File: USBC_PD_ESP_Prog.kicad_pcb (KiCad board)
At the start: 2 copper layers, 25 x 25 mm, 16 parts, among them J1 USB_C_Receptacle, J2 Conn_02x06_Counter_Clockwise, Q1 BC847, Q2 BC847, U1 FUSB302B01MPX, U2 CH340C, U3 NCP1117-3.3_SOT223

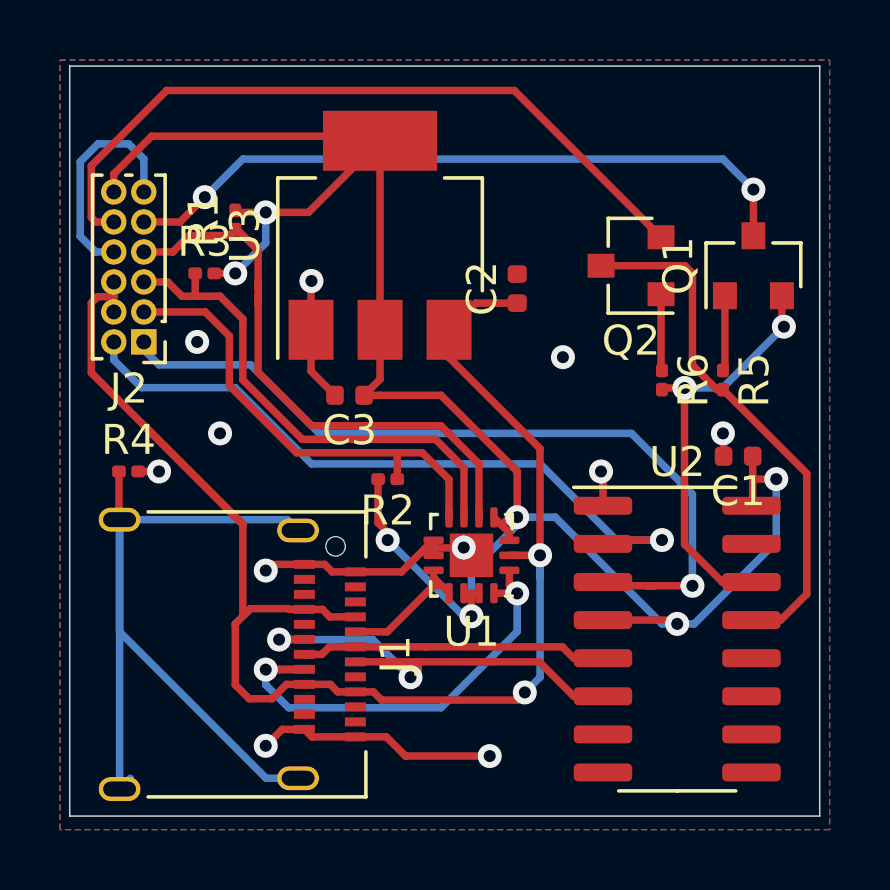
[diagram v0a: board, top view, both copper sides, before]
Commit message: Clean silkscreen
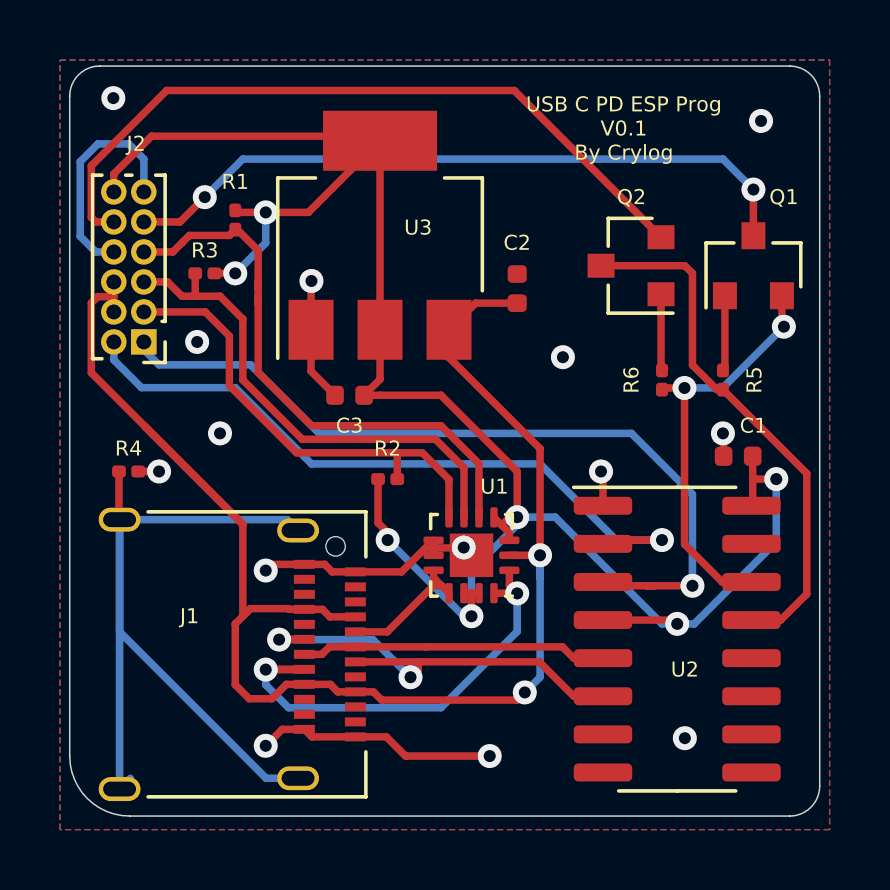
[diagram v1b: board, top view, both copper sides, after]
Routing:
- net GND: vias 11 -> 14
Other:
- outline, holes or cut-outs redrawn
- board text added: "USB C PD ESP Prog V0.1 By Crylog"
